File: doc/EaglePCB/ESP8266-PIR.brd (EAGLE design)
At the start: 72.1 x 40.6 mm, 10 parts, among them IC2 DS1820, IC3 LM340S

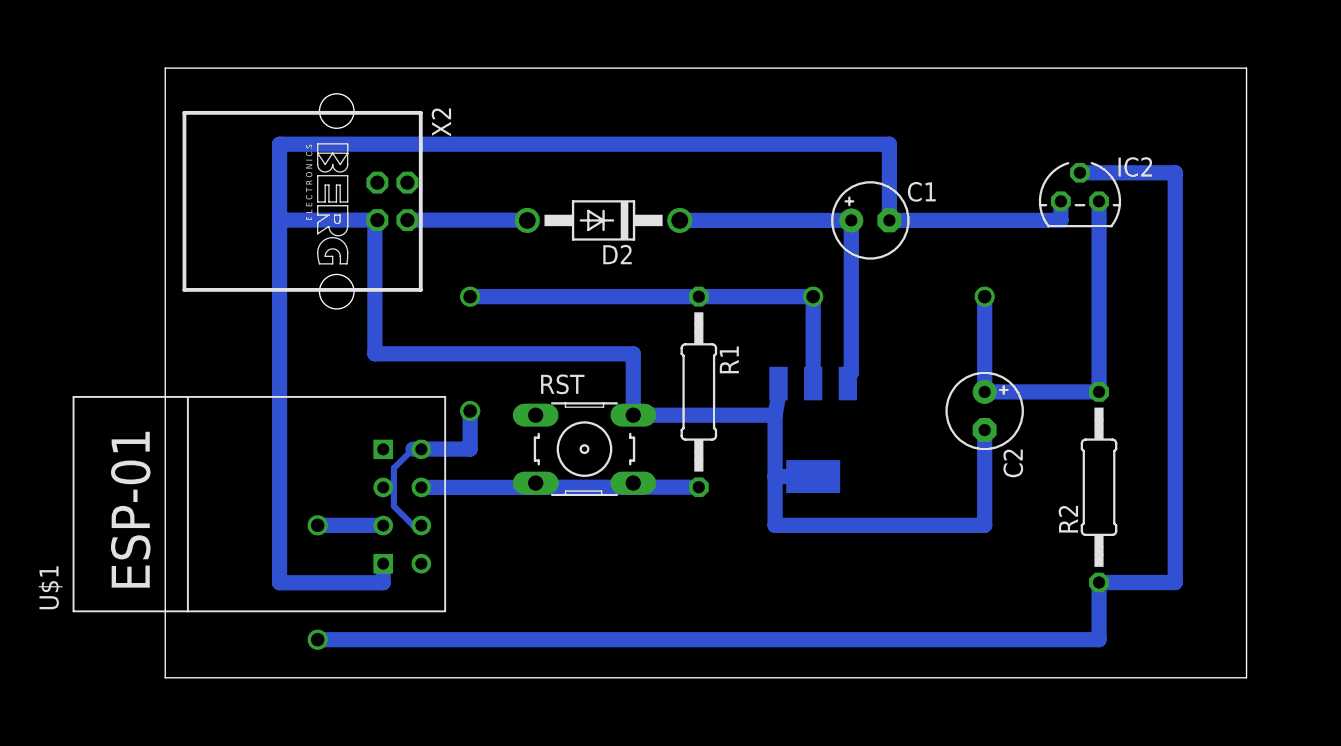
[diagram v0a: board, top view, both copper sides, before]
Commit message: correct PCB design and add PIR IoT device
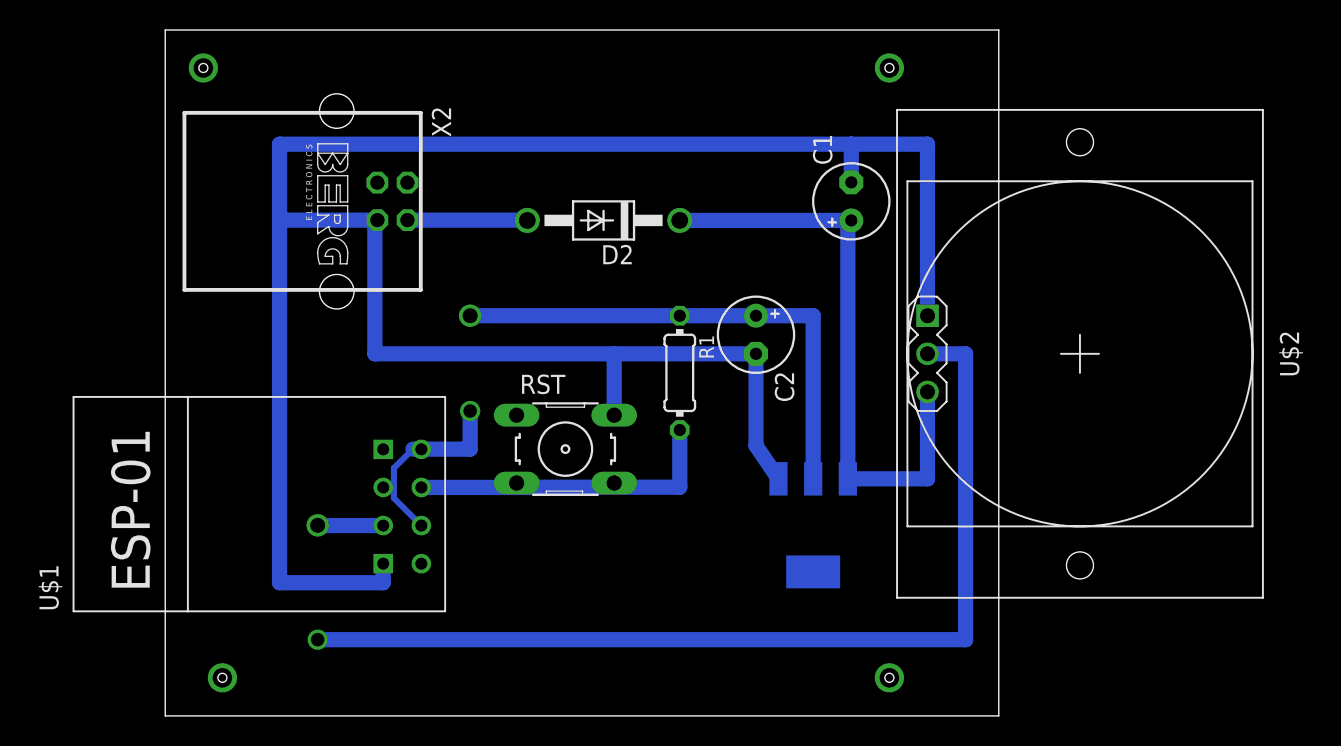
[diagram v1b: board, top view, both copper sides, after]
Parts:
- removed IC2: DS1820, DS1820:TO-92
- removed R2: 4.7k, resistor:0207/12
- added U$2: MOTION-PIR-DYP-ME003, diy-modules:MOTION-PIR-DYP-ME003
- R1: device resistor:0207/12 -> eagle-ltspice:0204/7
- moved C2 16.1 mm to (40.6, 59.7)
- moved IC3 6.35 mm to (44.5, 47.0)
- moved C1 1.80 mm to (47.0, 68.6), turned to 90 degrees
- moved R1 1.80 mm to (35.6, 57.1)
- moved RST 1.27 mm to (27.9, 52.1)
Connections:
- removed net DQ: IC2.2, R2.1, U$1.GPIO2
- new net GPIO2: U$1.GPIO2, U$2.2
- net 3V3: no longer IC2.3, R2.2
- net 5V: now also U$2.3
- net GND: now also U$2.1; no longer IC2.1
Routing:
- net DQ: track 99.0 -> 0.00 mm, vias 1 -> 0
- net GPIO2: track 0.00 -> 69.1 mm
- net GND: track 174.5 -> 148.4 mm
- net 3V3: track 69.5 -> 47.0 mm, vias 4 -> 1
- net 5V: track 30.5 -> 47.5 mm
- net N$4: track 18.8 -> 23.1 mm
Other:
- board size 72.1 x 40.6 mm -> 55.5 x 45.7 mm
